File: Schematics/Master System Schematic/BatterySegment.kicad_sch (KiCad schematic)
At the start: 148 parts

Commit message: Updated all + annotations
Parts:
- renumbered BT1401 to BT380, BT1402 to BT381, BT1403 to BT382, BT1404 to BT383, BT1405 to BT384, BT1406 to BT385, BT1407 to BT386, BT1408 to BT387, BT1409 to BT388, BT1410 to BT389, BT1411 to BT390, BT1412 to BT391, BT1413 to BT392, BT1414 to BT393, BT1415 to BT394, BT1416 to BT395, BT1417 to BT396, BT1418 to BT397, BT1419 to BT398, BT1420 to BT399, BT1421 to BT400, BT1422 to BT401, BT1423 to BT402, BT1424 to BT403, BT1425 to BT404, BT1426 to BT405, BT1427 to BT406, BT1428 to BT407, BT1429 to BT408, BT1430 to BT409, BT1431 to BT410, BT1432 to BT411, BT1433 to BT412, BT1434 to BT413, BT1435 to BT414, BT1436 to BT415, BT1437 to BT416, BT1438 to BT417, BT1439 to BT418, BT1440 to BT419, BT1441 to BT420, BT1442 to BT421, BT1443 to BT422, BT1444 to BT423, BT1445 to BT424, BT1446 to BT425, BT1447 to BT426, BT1448 to BT427, BT1449 to BT428, BT1450 to BT429, BT1451 to BT430, BT1452 to BT431, BT1453 to BT432, BT1454 to BT433, BT1455 to BT434, BT1456 to BT435, BT1457 to BT436, BT1458 to BT437, BT1459 to BT438, BT1460 to BT439, BT1461 to BT440, BT1462 to BT441, BT1463 to BT442, BT1464 to BT443, BT1465 to BT444, BT1466 to BT445, BT1467 to BT446, BT1468 to BT447, BT1469 to BT448, BT1470 to BT449, BT1471 to BT450, BT1472 to BT451, BT1473 to BT452, BT1474 to BT453, BT1475 to BT454, BT1476 to BT455, BT1477 to BT456, BT1478 to BT457, BT1479 to BT458, BT1480 to BT459, BT1481 to BT460, BT1482 to BT461, BT1483 to BT462, BT1484 to BT463, BT1485 to BT464, BT1486 to BT465, BT1487 to BT466, BT1488 to BT467, BT1489 to BT468, BT1490 to BT469, BT1491 to BT470, BT1492 to BT471, BT1493 to BT472, BT1494 to BT473, BT1495 to BT474, BT1496 to BT475, BT1497 to BT476, BT1498 to BT477, BT1499 to BT478, BT1500 to BT479, BT1501 to BT480, BT1502 to BT481, BT1503 to BT482, BT1504 to BT483, BT1505 to BT484, BT1506 to BT485, BT1507 to BT486, BT1508 to BT487, BT1509 to BT488, BT1510 to BT489, BT1511 to BT490, BT1512 to BT491, BT1513 to BT492, BT1514 to BT493, BT1515 to BT494, BT1516 to BT495, BT1517 to BT496, BT1518 to BT497, BT1519 to BT498, BT1520 to BT499, BT1521 to BT500, BT1522 to BT501, BT1523 to BT502, BT1524 to BT503, BT1525 to BT504, BT1526 to BT505, TH1401 to TH67, TH1402 to TH68, TH1403 to TH69, TH1404 to TH70, TH1405 to TH71, TH1406 to TH72, TH1407 to TH73, TH1408 to TH74, TH1409 to TH75, TH1410 to TH76, TH1411 to TH77, TH1412 to TH78, TH1413 to TH79, TH1414 to TH80, TH1415 to TH81, TH1416 to TH82, TH1417 to TH83, TH1418 to TH84, TH1419 to TH85, TH1420 to TH86, TH1421 to TH87, TH1422 to TH88

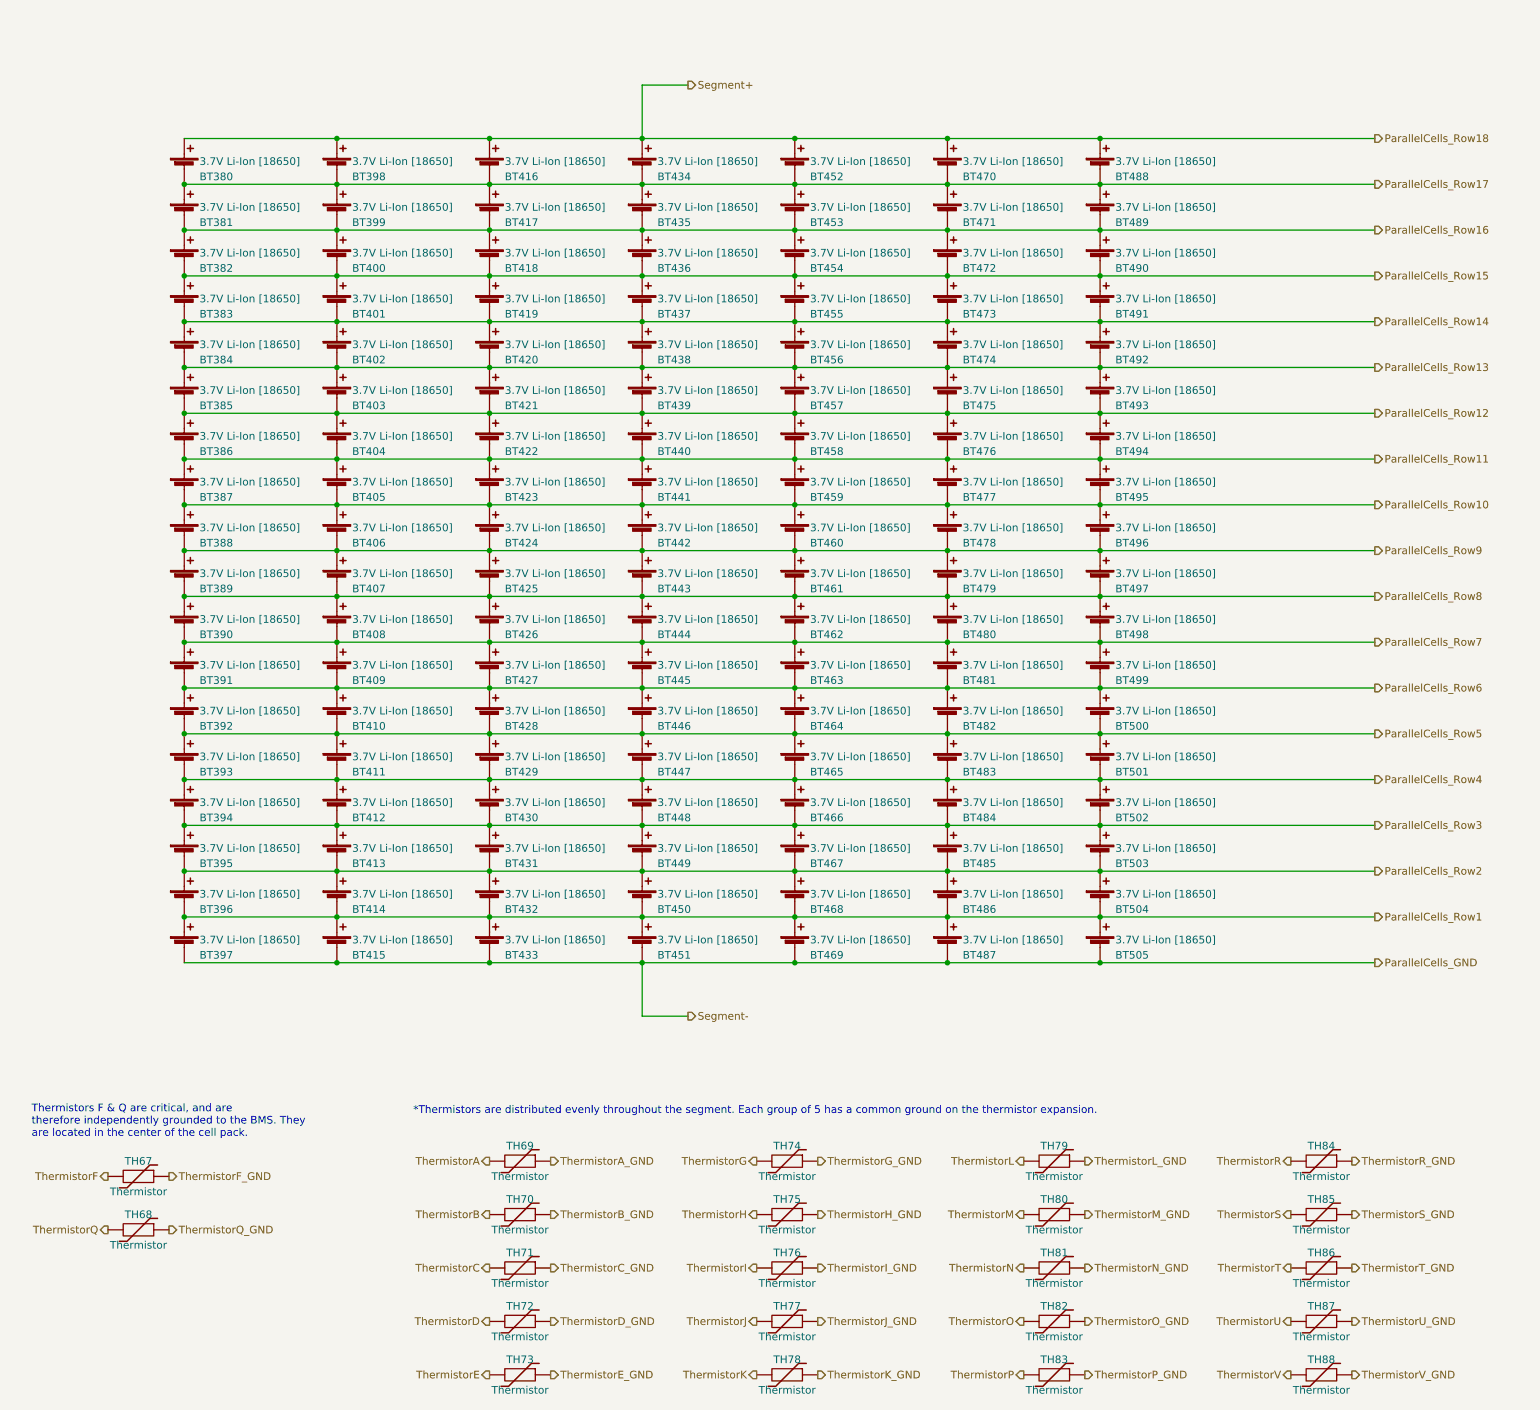
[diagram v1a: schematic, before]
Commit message: Footwell integration fix (#113)
* Beginning footwell fix

adding in

* Finished box, doing celeanup

* Cleaning up can wires

* Added non critical power

* Added misc indicators

* replaced old chassis markers

* fixing pin input/output/passive status

* Consolidation (part 1)

* Consolidation (part 2)

* Consolidation part 3 complete

#Scope creep

* weird autosave issue

* Fixing pin directions and grounds

* adding notations

* Adding CAN latching circuitry

* Fixed pin directions, added can latch

* FINAL edits
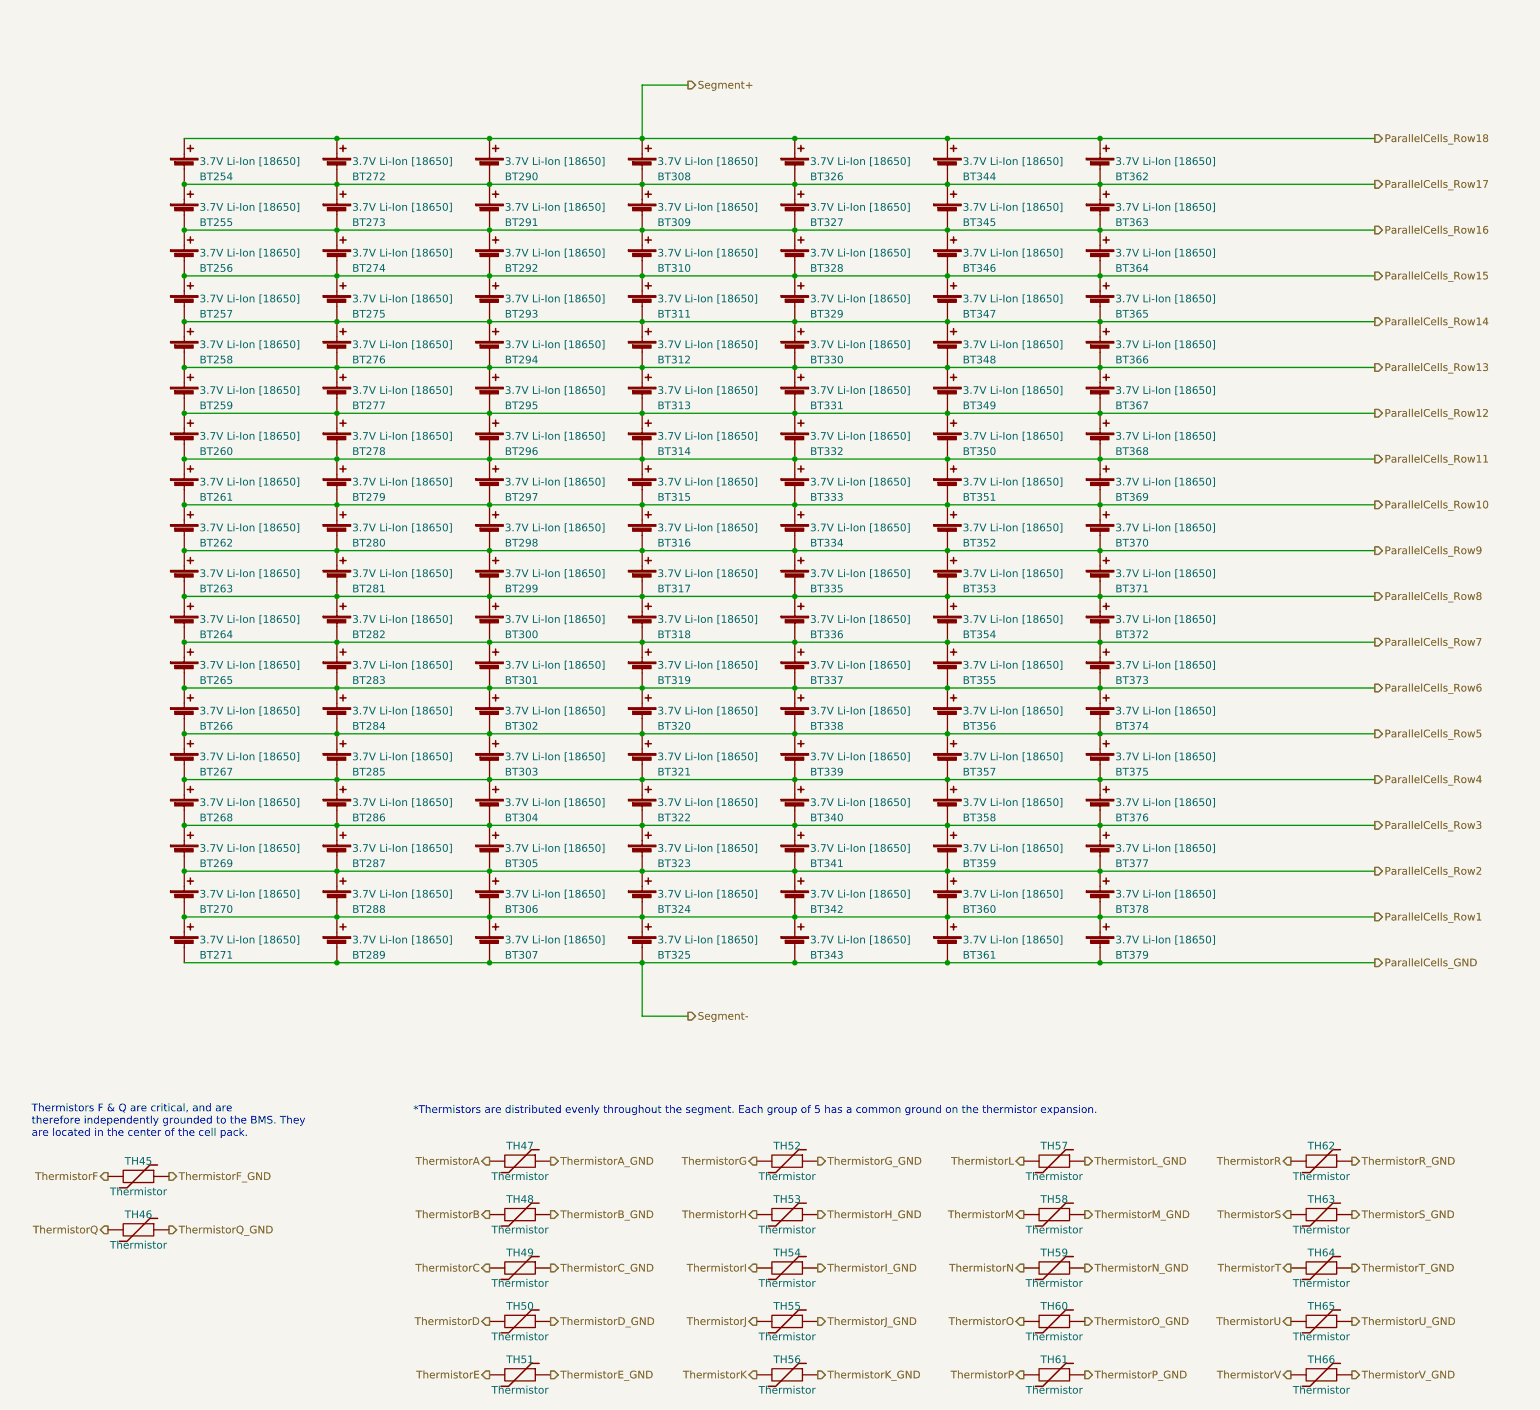
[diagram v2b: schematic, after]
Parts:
- renumbered BT380 to BT254, BT381 to BT255, BT382 to BT256, BT383 to BT257, BT384 to BT258, BT385 to BT259, BT386 to BT260, BT387 to BT261, BT388 to BT262, BT389 to BT263, BT390 to BT264, BT391 to BT265, BT392 to BT266, BT393 to BT267, BT394 to BT268, BT395 to BT269, BT396 to BT270, BT397 to BT271, BT398 to BT272, BT399 to BT273, BT400 to BT274, BT401 to BT275, BT402 to BT276, BT403 to BT277, BT404 to BT278, BT405 to BT279, BT406 to BT280, BT407 to BT281, BT408 to BT282, BT409 to BT283, BT410 to BT284, BT411 to BT285, BT412 to BT286, BT413 to BT287, BT414 to BT288, BT415 to BT289, BT416 to BT290, BT417 to BT291, BT418 to BT292, BT419 to BT293, BT420 to BT294, BT421 to BT295, BT422 to BT296, BT423 to BT297, BT424 to BT298, BT425 to BT299, BT426 to BT300, BT427 to BT301, BT428 to BT302, BT429 to BT303, BT430 to BT304, BT431 to BT305, BT432 to BT306, BT433 to BT307, BT434 to BT308, BT435 to BT309, BT436 to BT310, BT437 to BT311, BT438 to BT312, BT439 to BT313, BT440 to BT314, BT441 to BT315, BT442 to BT316, BT443 to BT317, BT444 to BT318, BT445 to BT319, BT446 to BT320, BT447 to BT321, BT448 to BT322, BT449 to BT323, BT450 to BT324, BT451 to BT325, BT452 to BT326, BT453 to BT327, BT454 to BT328, BT455 to BT329, BT456 to BT330, BT457 to BT331, BT458 to BT332, BT459 to BT333, BT460 to BT334, BT461 to BT335, BT462 to BT336, BT463 to BT337, BT464 to BT338, BT465 to BT339, BT466 to BT340, BT467 to BT341, BT468 to BT342, BT469 to BT343, BT470 to BT344, BT471 to BT345, BT472 to BT346, BT473 to BT347, BT474 to BT348, BT475 to BT349, BT476 to BT350, BT477 to BT351, BT478 to BT352, BT479 to BT353, BT480 to BT354, BT481 to BT355, BT482 to BT356, BT483 to BT357, BT484 to BT358, BT485 to BT359, BT486 to BT360, BT487 to BT361, BT488 to BT362, BT489 to BT363, BT490 to BT364, BT491 to BT365, BT492 to BT366, BT493 to BT367, BT494 to BT368, BT495 to BT369, BT496 to BT370, BT497 to BT371, BT498 to BT372, BT499 to BT373, BT500 to BT374, BT501 to BT375, BT502 to BT376, BT503 to BT377, BT504 to BT378, BT505 to BT379, TH67 to TH45, TH68 to TH46, TH69 to TH47, TH70 to TH48, TH71 to TH49, TH72 to TH50, TH73 to TH51, TH74 to TH52, TH75 to TH53, TH76 to TH54, TH77 to TH55, TH78 to TH56, TH79 to TH57, TH80 to TH58, TH81 to TH59, TH82 to TH60, TH83 to TH61, TH84 to TH62, TH85 to TH63, TH86 to TH64, TH87 to TH65, TH88 to TH66

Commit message: Dylan cleanup and continualupdates (#114)
* Annotations

* Added custom Chassis GND symbol
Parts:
- renumbered BT254 to BT380, BT255 to BT381, BT256 to BT382, BT257 to BT383, BT258 to BT384, BT259 to BT385, BT260 to BT386, BT261 to BT387, BT262 to BT388, BT263 to BT389, BT264 to BT390, BT265 to BT391, BT266 to BT392, BT267 to BT393, BT268 to BT394, BT269 to BT395, BT270 to BT396, BT271 to BT397, BT272 to BT398, BT273 to BT399, BT274 to BT400, BT275 to BT401, BT276 to BT402, BT277 to BT403, BT278 to BT404, BT279 to BT405, BT280 to BT406, BT281 to BT407, BT282 to BT408, BT283 to BT409, BT284 to BT410, BT285 to BT411, BT286 to BT412, BT287 to BT413, BT288 to BT414, BT289 to BT415, BT290 to BT416, BT291 to BT417, BT292 to BT418, BT293 to BT419, BT294 to BT420, BT295 to BT421, BT296 to BT422, BT297 to BT423, BT298 to BT424, BT299 to BT425, BT300 to BT426, BT301 to BT427, BT302 to BT428, BT303 to BT429, BT304 to BT430, BT305 to BT431, BT306 to BT432, BT307 to BT433, BT308 to BT434, BT309 to BT435, BT310 to BT436, BT311 to BT437, BT312 to BT438, BT313 to BT439, BT314 to BT440, BT315 to BT441, BT316 to BT442, BT317 to BT443, BT318 to BT444, BT319 to BT445, BT320 to BT446, BT321 to BT447, BT322 to BT448, BT323 to BT449, BT324 to BT450, BT325 to BT451, BT326 to BT452, BT327 to BT453, BT328 to BT454, BT329 to BT455, BT330 to BT456, BT331 to BT457, BT332 to BT458, BT333 to BT459, BT334 to BT460, BT335 to BT461, BT336 to BT462, BT337 to BT463, BT338 to BT464, BT339 to BT465, BT340 to BT466, BT341 to BT467, BT342 to BT468, BT343 to BT469, BT344 to BT470, BT345 to BT471, BT346 to BT472, BT347 to BT473, BT348 to BT474, BT349 to BT475, BT350 to BT476, BT351 to BT477, BT352 to BT478, BT353 to BT479, BT354 to BT480, BT355 to BT481, BT356 to BT482, BT357 to BT483, BT358 to BT484, BT359 to BT485, BT360 to BT486, BT361 to BT487, BT362 to BT488, BT363 to BT489, BT364 to BT490, BT365 to BT491, BT366 to BT492, BT367 to BT493, BT368 to BT494, BT369 to BT495, BT370 to BT496, BT371 to BT497, BT372 to BT498, BT373 to BT499, BT374 to BT500, BT375 to BT501, BT376 to BT502, BT377 to BT503, BT378 to BT504, BT379 to BT505, TH45 to TH67, TH46 to TH68, TH47 to TH69, TH48 to TH70, TH49 to TH71, TH50 to TH72, TH51 to TH73, TH52 to TH74, TH53 to TH75, TH54 to TH76, TH55 to TH77, TH56 to TH78, TH57 to TH79, TH58 to TH80, TH59 to TH81, TH60 to TH82, TH61 to TH83, TH62 to TH84, TH63 to TH85, TH64 to TH86, TH65 to TH87, TH66 to TH88

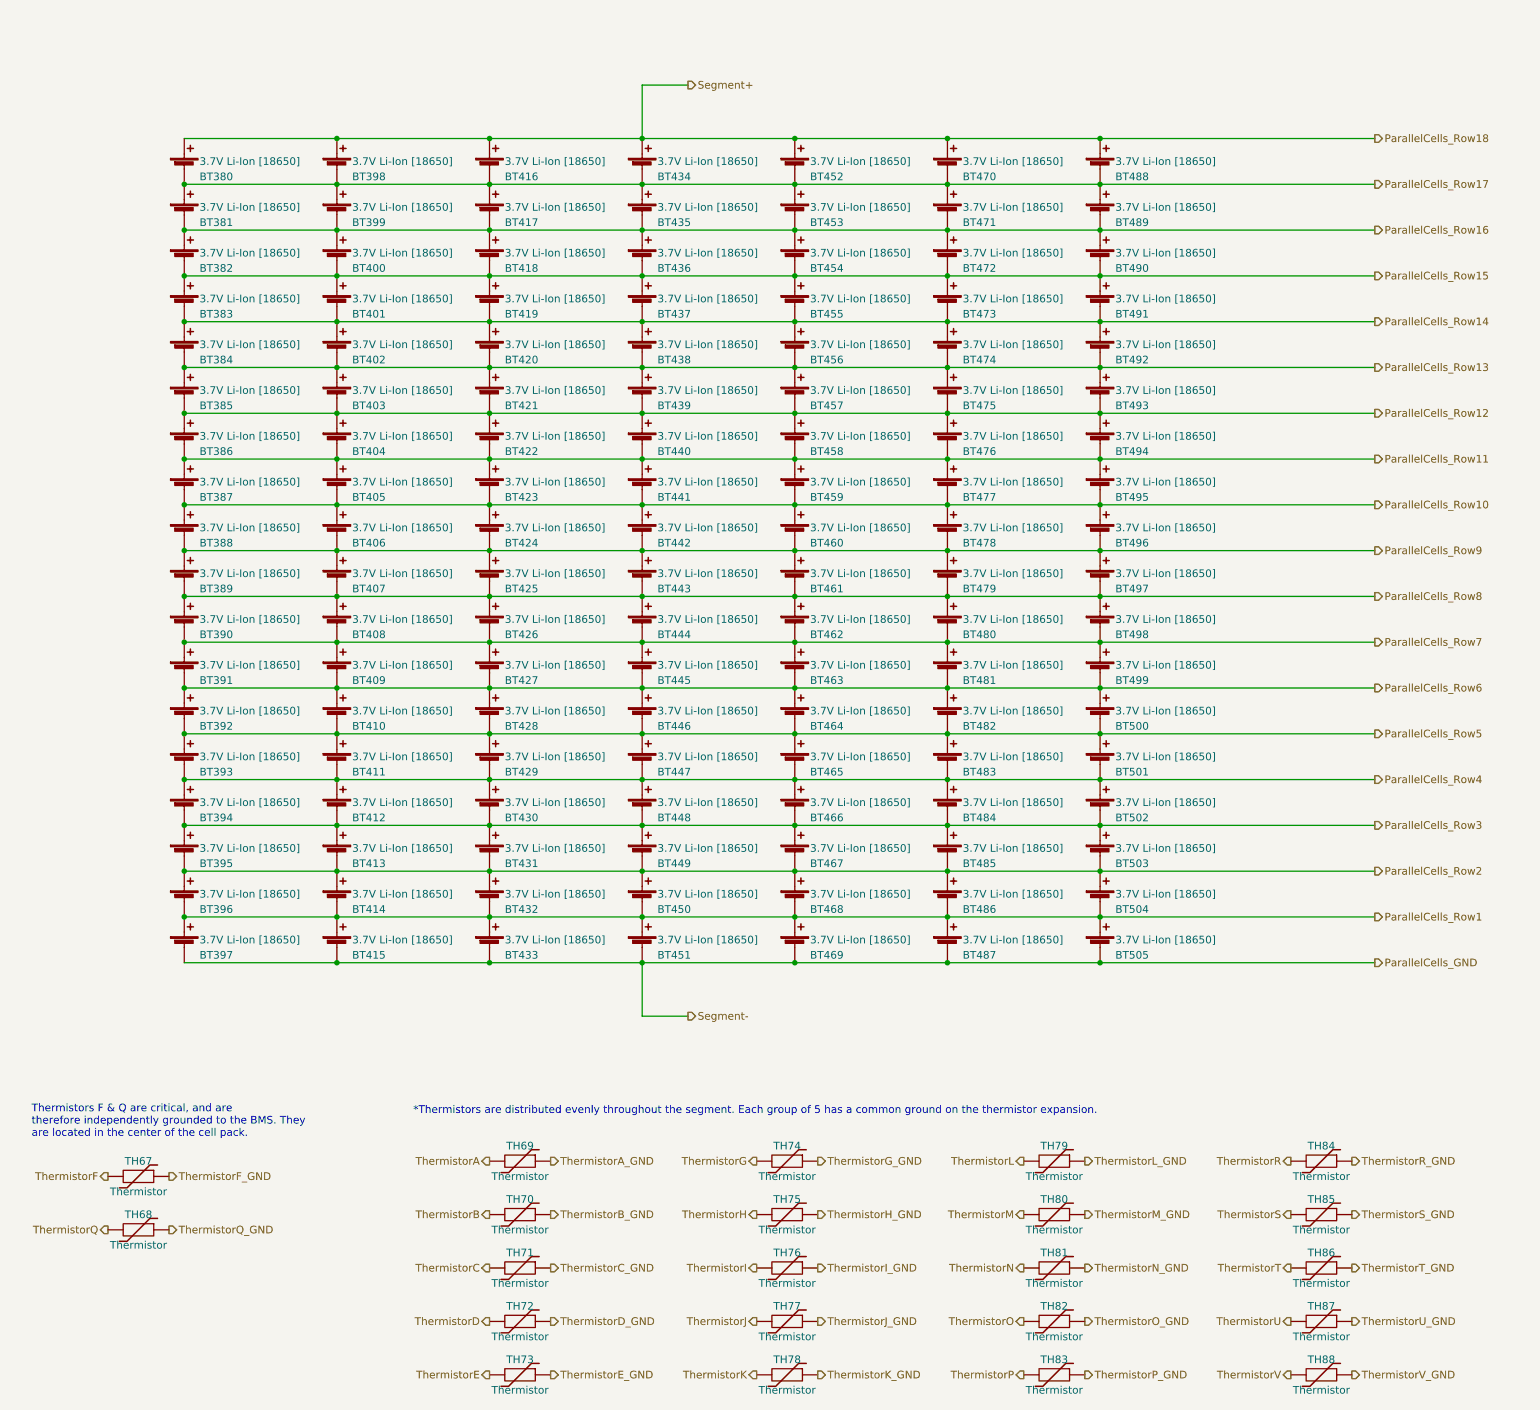
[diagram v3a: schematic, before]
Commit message: Update to accumulator and charger
Update to accumulator and charger color coding
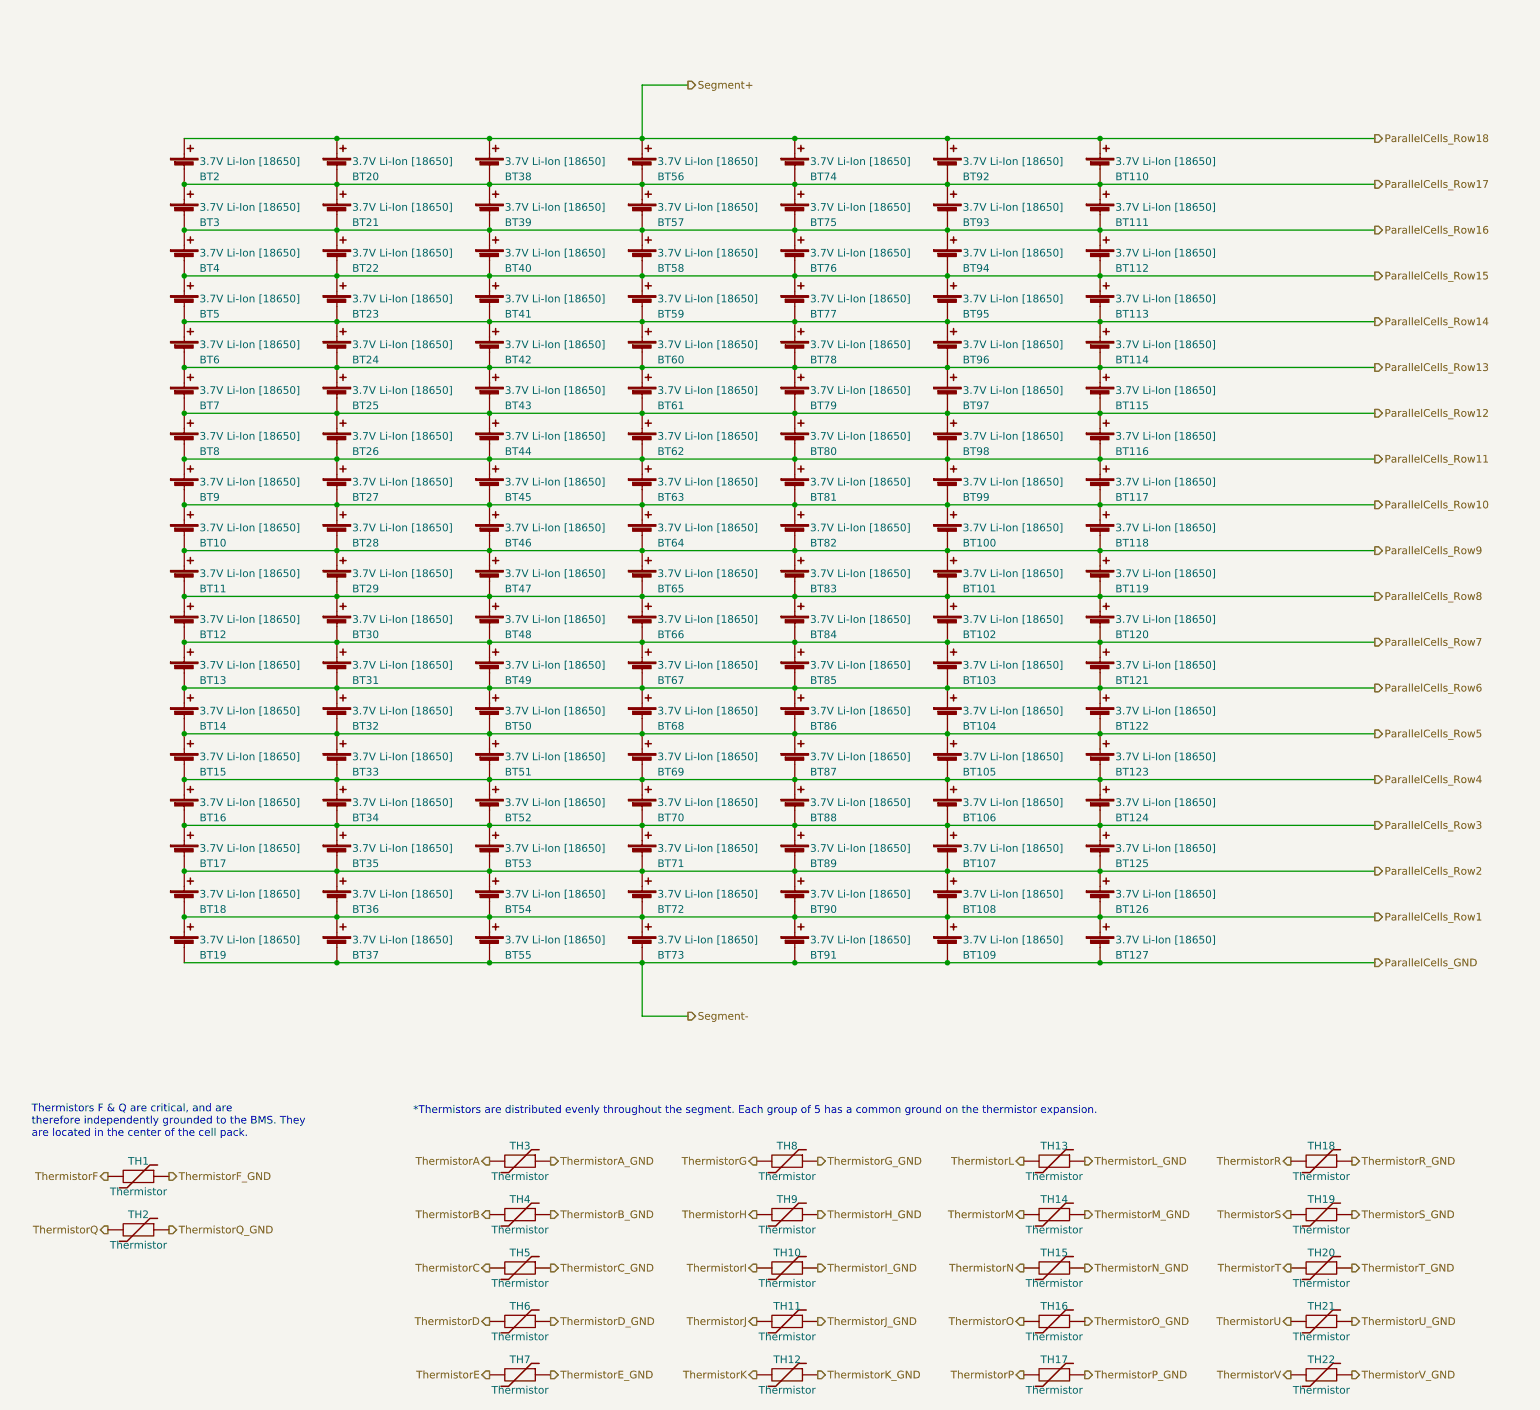
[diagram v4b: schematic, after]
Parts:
- renumbered BT388 to BT10, BT478 to BT100, BT479 to BT101, BT480 to BT102, BT481 to BT103, BT482 to BT104, BT483 to BT105, BT484 to BT106, BT485 to BT107, BT486 to BT108, BT487 to BT109, BT389 to BT11, BT488 to BT110, BT489 to BT111, BT490 to BT112, BT491 to BT113, BT492 to BT114, BT493 to BT115, BT494 to BT116, BT495 to BT117, BT496 to BT118, BT497 to BT119, BT390 to BT12, BT498 to BT120, BT499 to BT121, BT500 to BT122, BT501 to BT123, BT502 to BT124, BT503 to BT125, BT504 to BT126, BT505 to BT127, BT391 to BT13, BT392 to BT14, BT393 to BT15, BT394 to BT16, BT395 to BT17, BT396 to BT18, BT397 to BT19, BT380 to BT2, BT398 to BT20, BT399 to BT21, BT400 to BT22, BT401 to BT23, BT402 to BT24, BT403 to BT25, BT404 to BT26, BT405 to BT27, BT406 to BT28, BT407 to BT29, BT381 to BT3, BT408 to BT30, BT409 to BT31, BT410 to BT32, BT411 to BT33, BT412 to BT34, BT413 to BT35, BT414 to BT36, BT415 to BT37, BT416 to BT38, BT417 to BT39, BT382 to BT4, BT418 to BT40, BT419 to BT41, BT420 to BT42, BT421 to BT43, BT422 to BT44, BT423 to BT45, BT424 to BT46, BT425 to BT47, BT426 to BT48, BT427 to BT49, BT383 to BT5, BT428 to BT50, BT429 to BT51, BT430 to BT52, BT431 to BT53, BT432 to BT54, BT433 to BT55, BT434 to BT56, BT435 to BT57, BT436 to BT58, BT437 to BT59, BT384 to BT6, BT438 to BT60, BT439 to BT61, BT440 to BT62, BT441 to BT63, BT442 to BT64, BT443 to BT65, BT444 to BT66, BT445 to BT67, BT446 to BT68, BT447 to BT69, BT385 to BT7, BT448 to BT70, BT449 to BT71, BT450 to BT72, BT451 to BT73, BT452 to BT74, BT453 to BT75, BT454 to BT76, BT455 to BT77, BT456 to BT78, BT457 to BT79, BT386 to BT8, BT458 to BT80, BT459 to BT81, BT460 to BT82, BT461 to BT83, BT462 to BT84, BT463 to BT85, BT464 to BT86, BT465 to BT87, BT466 to BT88, BT467 to BT89, BT387 to BT9, BT468 to BT90, BT469 to BT91, BT470 to BT92, BT471 to BT93, BT472 to BT94, BT473 to BT95, BT474 to BT96, BT475 to BT97, BT476 to BT98, BT477 to BT99, TH67 to TH1, TH76 to TH10, TH77 to TH11, TH78 to TH12, TH79 to TH13, TH80 to TH14, TH81 to TH15, TH82 to TH16, TH83 to TH17, TH84 to TH18, TH85 to TH19, TH68 to TH2, TH86 to TH20, TH87 to TH21, TH88 to TH22, TH69 to TH3, TH70 to TH4, TH71 to TH5, TH72 to TH6, TH73 to TH7, TH74 to TH8, TH75 to TH9

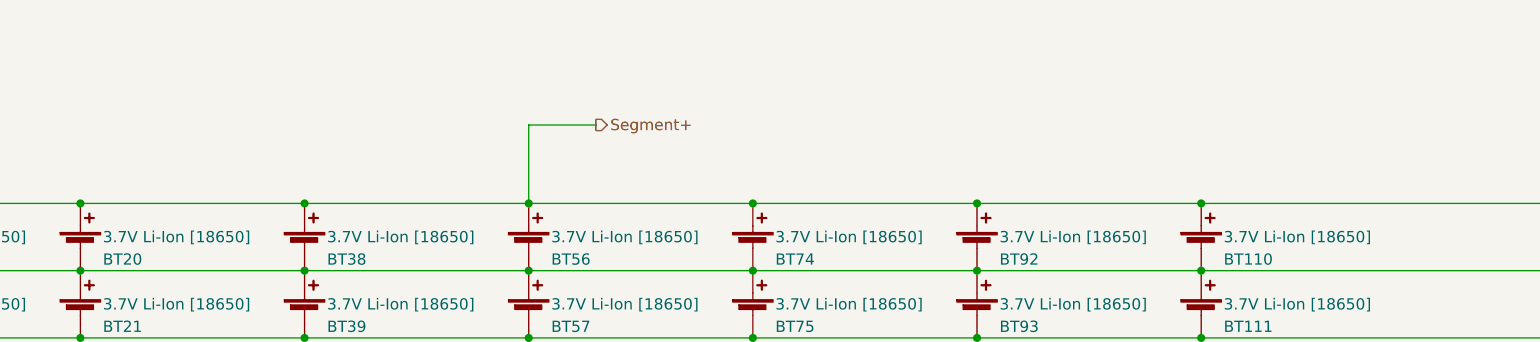
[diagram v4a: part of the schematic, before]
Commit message: Update color coding
Update color coding accumulator stuff
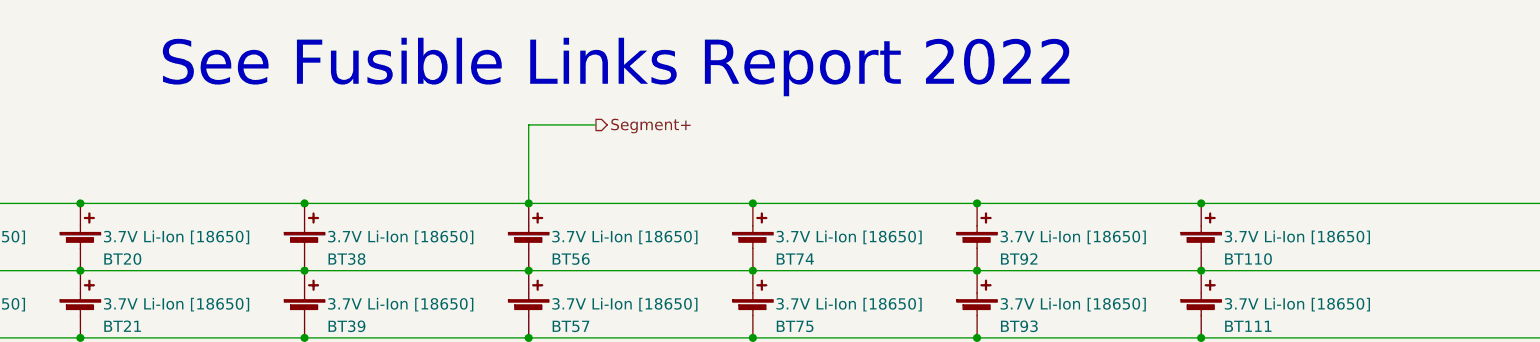
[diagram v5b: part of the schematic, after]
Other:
- note added: "See Fusible Links Report 2022"
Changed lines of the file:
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@@
     (effects (font (size 1.27 1.27)) (justify left bottom))
+  )
+  (text "See Fusible Links Report 2022" (at 102.87 24.13 0)
+    (effects (font (size 5 5)) (justify left bottom))
   )
   (text "*Thermistors are distributed evenly throughout the segment. Each group of 5 has a common ground on the thermistor expansion."
